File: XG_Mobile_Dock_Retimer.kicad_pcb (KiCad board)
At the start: 4 copper layers, 220.1 x 93 mm, 138 parts, among them J1 5-1775443-8, J10 SWD, J11 UART, J12 I2C1, J13 39301240, J14 SWD, J15 SWD, J17 8730, J2 20455-040E-76, J20 SWD, J21 SWD, J22 SWD, J23 SWD, J24 SWD, J25 SWD, J26 SWD, J27 SWD, J28 SWD, J29 SWD, J3 20455-040E-76, J30 SWD, J31 SWD, J32 SWD, J33 SWD, J4 3-2362375-4, J5 USB_C_Receptacle, J6 455860005, Q16 AO3401A, Q17 2N7002W, SW1 SW_Push, U1 DS160PT801ACBR, U12 STM32F030C8Tx

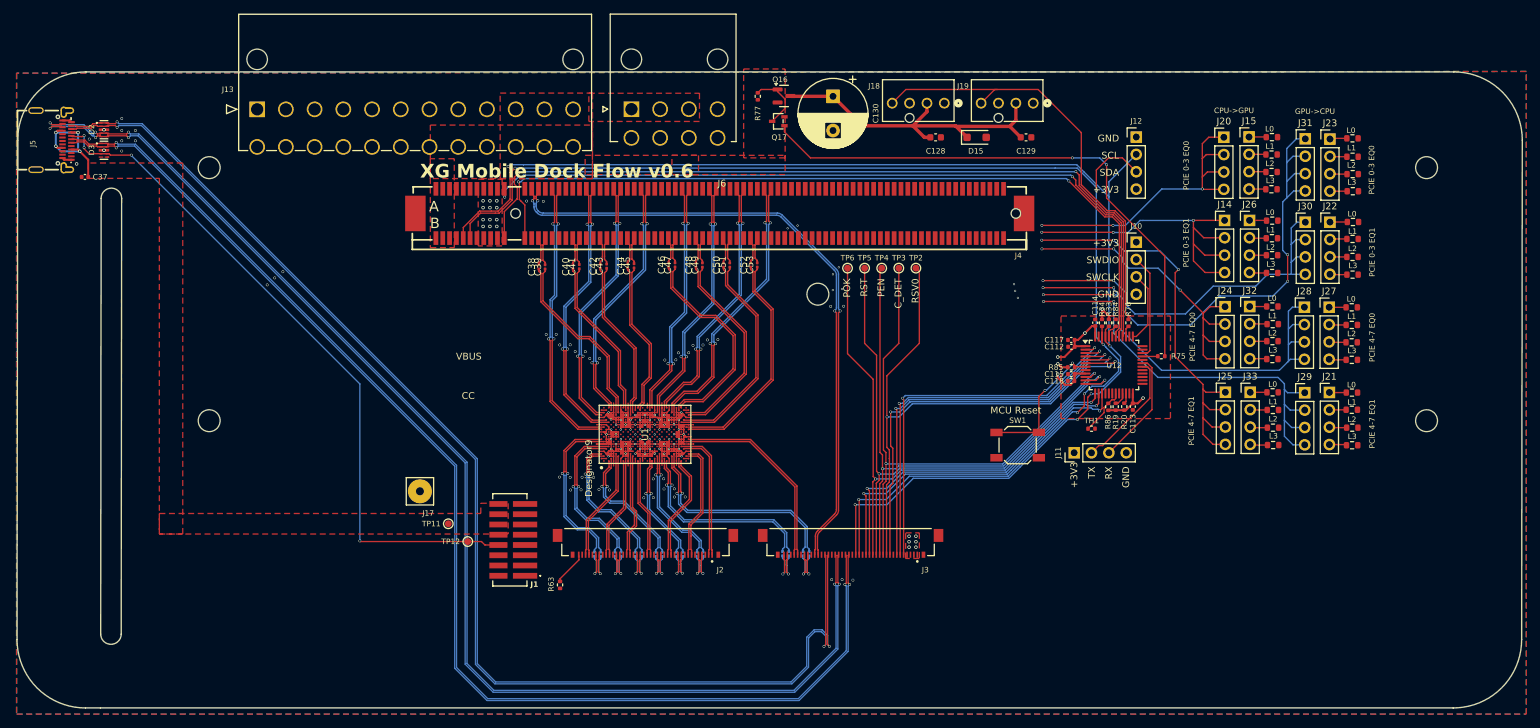
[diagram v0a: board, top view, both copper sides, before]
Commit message: try to route power to retimer
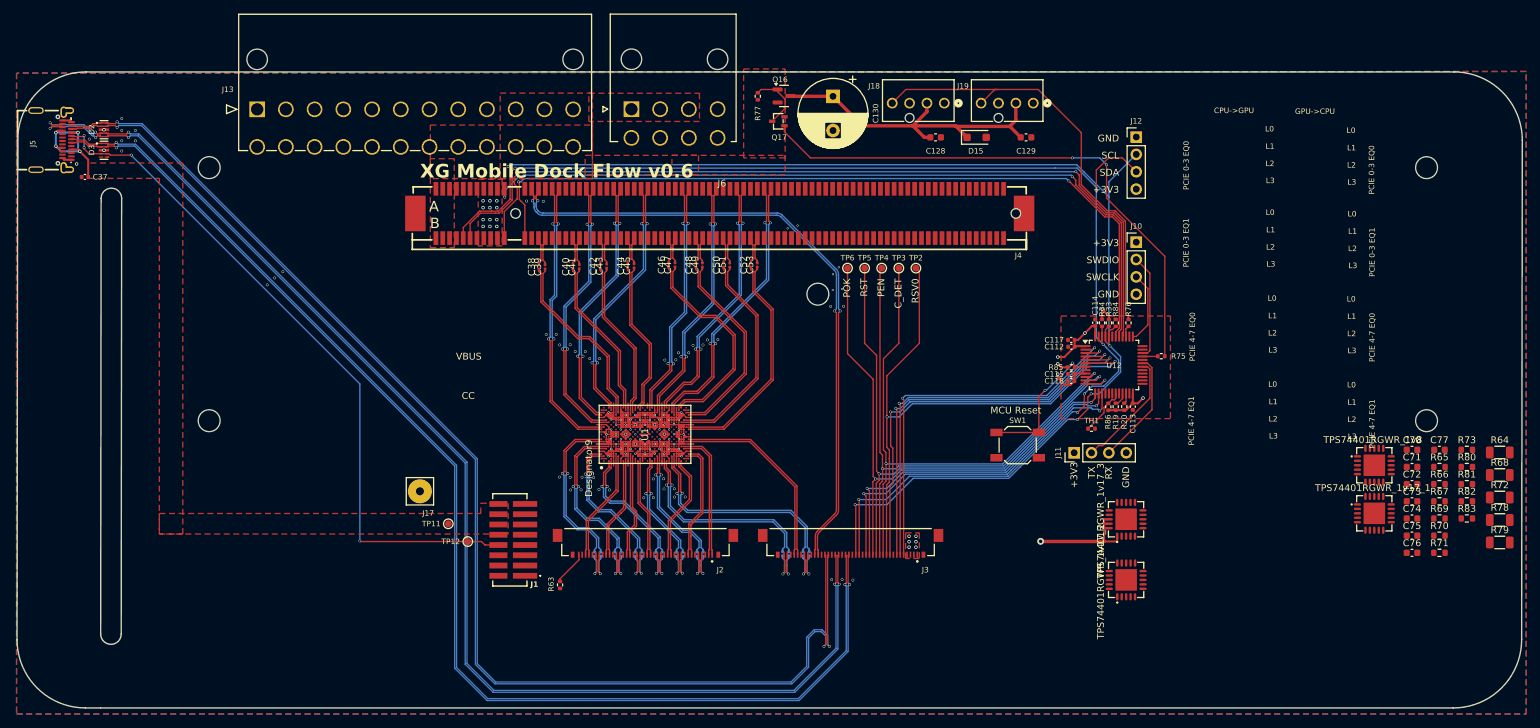
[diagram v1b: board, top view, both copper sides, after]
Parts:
- removed J14, J15, J20, J21, J22, J23, J24, J25, J26, J27, J28, J29, J30, J31, J32, J33: SWD, Connector_PinHeader_2.54mm:PinHeader_1x04_P2.54mm_Vertical
- removed R100, R104, R88, R92, R96: 75k, Resistor_SMD:R_0603_1608Metric
- removed R101, R89, R93, R97: 1k, Resistor_SMD:R_0603_1608Metric
- removed R102, R90, R94, R98: 8.25k, Resistor_SMD:R_0603_1608Metric
- removed R103, R87, R91, R95, R99: 24.9k, Resistor_SMD:R_0603_1608Metric
- added C70: 4.7μF, Capacitor_SMD:C_0603_1608Metric, F.Cu at (220.7, 94.7)
- added C71: 4.7μF, Capacitor_SMD:C_0603_1608Metric, F.Cu at (220.7, 97.2)
- added C72: 4.7μF, Capacitor_SMD:C_0603_1608Metric, F.Cu at (220.7, 99.7)
- added C73: 4.7μF, Capacitor_SMD:C_0603_1608Metric, F.Cu at (220.7, 102.2)
- added C74: 4.7μF, Capacitor_SMD:C_0603_1608Metric, F.Cu at (220.7, 104.7)
- added C75: 4.7μF, Capacitor_SMD:C_0603_1608Metric, F.Cu at (220.7, 107.2)
- added C76: 4.7μF, Capacitor_SMD:C_0603_1608Metric, F.Cu at (220.7, 109.7)
- added C77: 4.7μF, Capacitor_SMD:C_0603_1608Metric, F.Cu at (224.7, 94.7)
- added R64: 1k, Resistor_SMD:R_1206_3216Metric, F.Cu at (233.5, 95.1)
- added R65: 430, Resistor_SMD:R_0603_1608Metric, F.Cu at (224.7, 97.2)
- added TPS74401RGWR_1v17_1: ~, VQFN-20_L5.0-W5.0-P0.65-TL-EP:VQFN-20_L5.0-W5.0-P0.65-TL-EP, F.Cu at (215.2, 104.0)
- added TPS74401RGWR_1v17_2: ~, VQFN-20_L5.0-W5.0-P0.65-TL-EP:VQFN-20_L5.0-W5.0-P0.65-TL-EP, F.Cu at (178.9, 113.7)
- added TPS74401RGWR_1v17_3: ~, VQFN-20_L5.0-W5.0-P0.65-TL-EP:VQFN-20_L5.0-W5.0-P0.65-TL-EP, F.Cu at (178.8, 104.8)
- added TPS74401RGWR_1v8: ~, VQFN-20_L5.0-W5.0-P0.65-TL-EP:VQFN-20_L5.0-W5.0-P0.65-TL-EP, F.Cu at (215.2, 96.9)
- R66, R70: value 1k -> 30
- R67, R71: value 8.25k -> 3
- R68, R72: value 24.9k -> 1k; footprint Resistor_SMD:R_0603_1608Metric -> Resistor_SMD:R_1206_3216Metric
- R69, R73: value 75k -> 430
- R78: footprint Resistor_SMD:R_0603_1608Metric -> Resistor_SMD:R_1206_3216Metric
- R79: value 8.25k -> 1k; footprint Resistor_SMD:R_0603_1608Metric -> Resistor_SMD:R_1206_3216Metric
- R80: value 24.9k -> 30
- R81: value 75k -> 3
- R82: value 1k -> 240
- R83: value 8.25k -> 10
- moved R66 56.3 mm to (224.7, 99.7), turned to 0 degrees
- moved R67 56.3 mm to (224.7, 102.2), turned to 0 degrees
- moved R68 55.5 mm to (233.5, 98.4), turned to 0 degrees
- moved R69 54.0 mm to (224.7, 104.7), turned to 0 degrees
- moved R79 46.1 mm to (233.5, 108.2), turned to 0 degrees
- moved R78 45.6 mm to (233.5, 104.9), turned to 0 degrees
- moved R80 33.9 mm to (228.7, 97.2), turned to 0 degrees
- moved R81 33.8 mm to (228.7, 99.7), turned to 0 degrees
- moved R82 32.6 mm to (228.7, 102.2), turned to 0 degrees
- moved R83 32.5 mm to (228.7, 104.7), turned to 0 degrees
- moved R71 24.5 mm to (224.7, 109.7), turned to 0 degrees
- moved R70 24.5 mm to (224.7, 107.2), turned to 0 degrees
- moved R72 23.9 mm to (233.5, 101.7), turned to 0 degrees
- moved R73 16.8 mm to (228.7, 94.7), turned to 0 degrees
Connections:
- R66 pad 1: GND -> Net-(R65-Pad1)
- R66 pad 2: Net-(J15-Pin_1) -> Net-(R66-Pad2)
- R67 pad 1: GND -> +1V17_1
- R67 pad 2: Net-(J15-Pin_2) -> Net-(R66-Pad2)
- R68 pad 1: GND -> Net-(TPS74401RGWR_1v17_2-FB)
- R68 pad 2: Net-(J15-Pin_3) -> GND
- R69 pad 1: GND -> Net-(R69-Pad1)
- R69 pad 2: Net-(J15-Pin_4) -> Net-(TPS74401RGWR_1v17_2-FB)
- R70 pad 1: GND -> Net-(R69-Pad1)
- R70 pad 2: Net-(J21-Pin_1) -> Net-(R70-Pad2)
- R71 pad 1: GND -> +1V17_2
- R71 pad 2: Net-(J21-Pin_2) -> Net-(R70-Pad2)
- R72 pad 1: GND -> Net-(TPS74401RGWR_1v17_3-FB)
- R72 pad 2: Net-(J21-Pin_3) -> GND
- R73 pad 1: GND -> Net-(R73-Pad1)
- R73 pad 2: Net-(J21-Pin_4) -> Net-(TPS74401RGWR_1v17_3-FB)
- R78 pad 1: GND -> Net-(TPS74401RGWR_1v8-FB)
- R78 pad 2: Net-(J32-Pin_1) -> GND
- R79 pad 1: GND -> Net-(R79-Pad1)
- R79 pad 2: Net-(J32-Pin_2) -> Net-(TPS74401RGWR_1v8-FB)
- R80 pad 1: GND -> Net-(R73-Pad1)
- R80 pad 2: Net-(J32-Pin_3) -> Net-(R80-Pad2)
- R81 pad 1: GND -> +1V17_3
- R81 pad 2: Net-(J32-Pin_4) -> Net-(R80-Pad2)
- R82 pad 1: GND -> Net-(R79-Pad1)
- R82 pad 2: Net-(J33-Pin_1) -> Net-(R82-Pad2)
- R83 pad 1: GND -> +1V8
- R83 pad 2: Net-(J33-Pin_2) -> Net-(R82-Pad2)
- U1 pad AA12: unconnected-(U1F-PWR2_HS_D-PadAA12) -> +1V17_2
- U1 pad AB15: unconnected-(U1F-PWR_2_A-PadAB15) -> +1V17_1
- U1 pad AB17: unconnected-(U1F-PWR_2_A-PadAB17) -> +1V17_1
- U1 pad AB7: unconnected-(U1F-PWR2_HS_A-PadAB7) -> +1V17_3
- U1 pad AB9: unconnected-(U1F-PWR2_HS_A-PadAB9) -> +1V17_3
- U1 pad AC10: unconnected-(U1F-PWR2_HS_D-PadAC10) -> +1V17_2
- U1 pad AC14: unconnected-(U1F-PWR_2_A-PadAC14) -> +1V17_1
- U1 pad AD15: unconnected-(U1F-PWR_2_A-PadAD15) -> +1V17_1
- U1 pad AD17: unconnected-(U1F-PWR_2_A-PadAD17) -> +1V17_1
- U1 pad AD7: unconnected-(U1F-PWR2_HS_A-PadAD7) -> +1V17_3
- U1 pad AD9: unconnected-(U1F-PWR2_HS_A-PadAD9) -> +1V17_3
- U1 pad AE12: unconnected-(U1C-PWR_1-PadAE12) -> +1V8
- U1 pad AF11: unconnected-(U1C-PWR_1-PadAF11) -> +1V8
- U1 pad AF13: unconnected-(U1C-PWR_1-PadAF13) -> +1V8
- U1 pad AG10: unconnected-(U1C-PWR_1-PadAG10) -> +1V8
- U1 pad AG14: unconnected-(U1C-PWR_1-PadAG14) -> +1V8
- U1 pad AH11: unconnected-(U1C-PWR_1-PadAH11) -> +1V8
- U1 pad AH13: unconnected-(U1C-PWR_1-PadAH13) -> +1V8
- U1 pad AJ12: unconnected-(U1C-PWR_1-PadAJ12) -> +1V8
- U1 pad AK15: unconnected-(U1F-PWR2_HS_D-PadAK15) -> +1V17_2
- U1 pad AK17: unconnected-(U1F-PWR2_HS_A-PadAK17) -> +1V17_3
- U1 pad AK7: unconnected-(U1F-PWR2_HS_A-PadAK7) -> +1V17_3
- U1 pad AK9: unconnected-(U1F-PWR2_HS_D-PadAK9) -> +1V17_2
- U1 pad AL10: unconnected-(U1F-PWR2_HS_D-PadAL10) -> +1V17_2
- U1 pad AL14: unconnected-(U1F-PWR2_HS_D-PadAL14) -> +1V17_2
- U1 pad AM15: unconnected-(U1F-PWR2_HS_D-PadAM15) -> +1V17_2
- U1 pad AM17: unconnected-(U1F-PWR2_HS_A-PadAM17) -> +1V17_3
- U1 pad AM7: unconnected-(U1F-PWR2_HS_A-PadAM7) -> +1V17_3
- U1 pad AM9: unconnected-(U1F-PWR2_HS_D-PadAM9) -> +1V17_2
- U1 pad F15: unconnected-(U1F-PWR2_HS_D-PadF15) -> +1V17_2
- U1 pad F17: unconnected-(U1F-PWR2_HS_A-PadF17) -> +1V17_3
- U1 pad F7: unconnected-(U1F-PWR2_HS_A-PadF7) -> +1V17_3
- U1 pad F9: unconnected-(U1F-PWR2_HS_D-PadF9) -> +1V17_2
- U1 pad G10: unconnected-(U1F-PWR2_HS_D-PadG10) -> +1V17_2
- U1 pad G14: unconnected-(U1F-PWR2_HS_D-PadG14) -> +1V17_2
- U1 pad H15: unconnected-(U1F-PWR2_HS_D-PadH15) -> +1V17_2
- U1 pad H17: unconnected-(U1F-PWR2_HS_A-PadH17) -> +1V17_3
- U1 pad H7: unconnected-(U1F-PWR2_HS_A-PadH7) -> +1V17_3
- U1 pad H9: unconnected-(U1F-PWR2_HS_D-PadH9) -> +1V17_2
- U1 pad J12: unconnected-(U1C-PWR_1-PadJ12) -> +1V8
- U1 pad K11: unconnected-(U1C-PWR_1-PadK11) -> +1V8
- U1 pad K13: unconnected-(U1C-PWR_1-PadK13) -> +1V8
- U1 pad L10: unconnected-(U1C-PWR_1-PadL10) -> +1V8
- U1 pad L14: unconnected-(U1C-PWR_1-PadL14) -> +1V8
- U1 pad M11: unconnected-(U1C-PWR_1-PadM11) -> +1V8
- U1 pad M13: unconnected-(U1C-PWR_1-PadM13) -> +1V8
- U1 pad N12: unconnected-(U1C-PWR_1-PadN12) -> +1V8
- U1 pad P15: unconnected-(U1F-PWR2_HS_A-PadP15) -> +1V17_3
- U1 pad P17: unconnected-(U1F-PWR2_HS_A-PadP17) -> +1V17_3
- U1 pad P7: unconnected-(U1F-PWR_2_A-PadP7) -> +1V17_1
- U1 pad P9: unconnected-(U1F-PWR_2_A-PadP9) -> +1V17_1
- U1 pad R10: unconnected-(U1F-PWR_2_A-PadR10) -> +1V17_1
- U1 pad R14: unconnected-(U1F-PWR2_HS_D-PadR14) -> +1V17_2
- U1 pad T15: unconnected-(U1F-PWR2_HS_A-PadT15) -> +1V17_3
- U1 pad T17: unconnected-(U1F-PWR2_HS_A-PadT17) -> +1V17_3
- U1 pad T7: unconnected-(U1F-PWR_2_A-PadT7) -> +1V17_1
- U1 pad T9: unconnected-(U1F-PWR_2_A-PadT9) -> +1V17_1
- U1 pad U12: unconnected-(U1F-PWR2_HS_D-PadU12) -> +1V17_2
- U1 pad V11: unconnected-(U1F-PWR2_HS_D-PadV11) -> +1V17_2
- U1 pad V13: unconnected-(U1F-PWR2_HS_A-PadV13) -> +1V17_3
- U1 pad W10: unconnected-(U1F-PWR2_HS_A-PadW10) -> +1V17_3
- U1 pad W14: unconnected-(U1F-PWR2_HS_A-PadW14) -> +1V17_3
- U1 pad Y11: unconnected-(U1F-PWR2_HS_A-PadY11) -> +1V17_3
- U1 pad Y13: unconnected-(U1F-PWR2_HS_D-PadY13) -> +1V17_2
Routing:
- net +1V17_3: track 0.00 -> 92.0 mm, vias 0 -> 3
- net /GPU_TO_CPU_EQ0_0: track 90.6 -> 0.00 mm, vias 4 -> 0
- net /GPU_TO_CPU_EQ1_1: track 79.5 -> 0.00 mm, vias 2 -> 0
- net /GPU_TO_CPU_EQ0_1: track 77.0 -> 0.00 mm, vias 2 -> 0
- net /GPU_TO_CPU_EQ1_0: track 73.8 -> 0.00 mm, vias 2 -> 0
- net /CPU_TO_GPU_EQ1_1: track 64.9 -> 0.00 mm, vias 3 -> 0
- net /CPU_TO_GPU_EQ1_0: track 51.6 -> 0.00 mm, vias 3 -> 0
- net /CPU_TO_GPU_EQ0_1: track 51.4 -> 0.00 mm, vias 3 -> 0
- net /CPU_TO_GPU_EQ0_0: track 51.3 -> 0.00 mm, vias 3 -> 0
- net +1V8: track 0.00 -> 17.7 mm, vias 0 -> 2
- net +1V17_1: track 0.00 -> 13.1 mm, vias 0 -> 2
- net GND: track 307.8 -> 301.6 mm, vias 127 -> 117
- net Net-(J22-Pin_2): track 2.58 -> 0.00 mm
- net Net-(J33-Pin_4): track 2.57 -> 0.00 mm
- net Net-(J32-Pin_2): track 2.55 -> 0.00 mm
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
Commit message: more changes to power zones
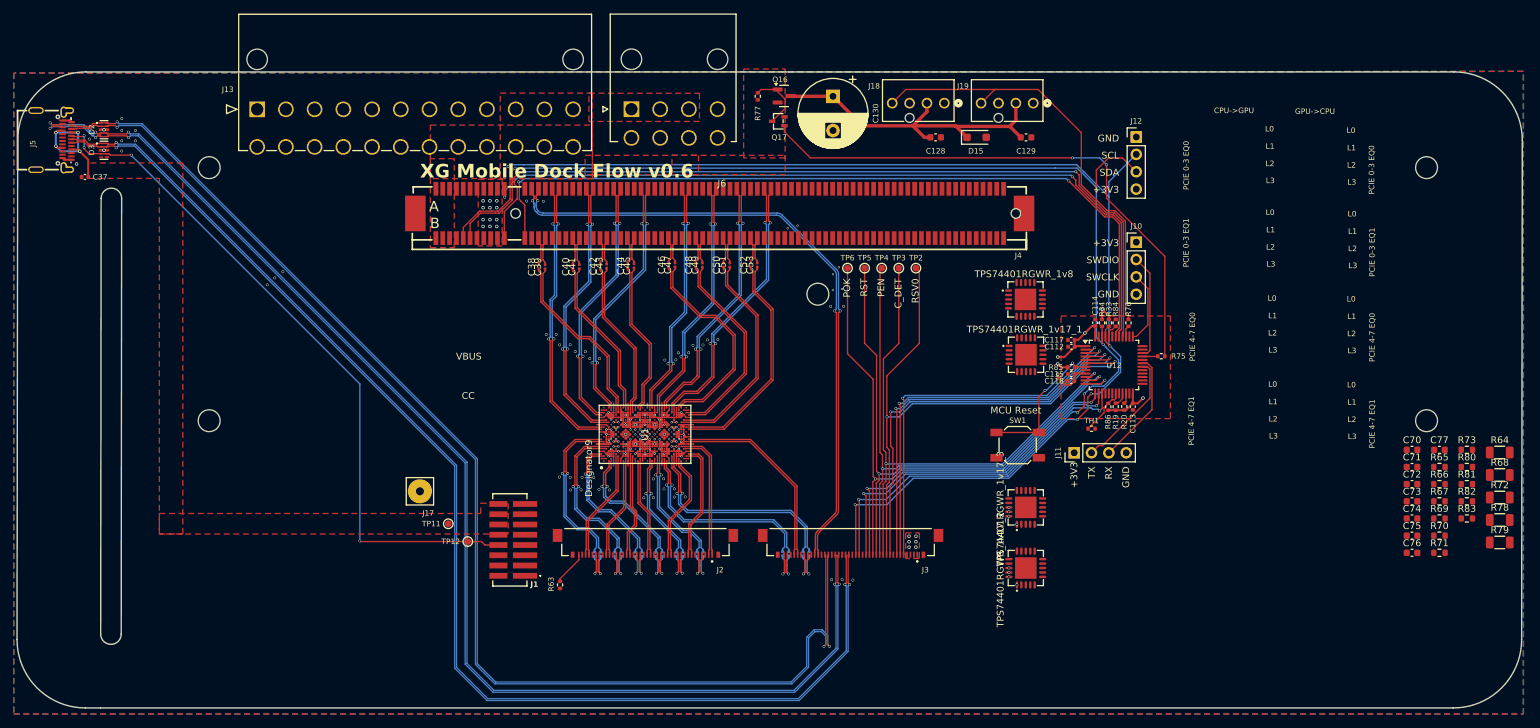
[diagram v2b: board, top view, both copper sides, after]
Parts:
- moved TPS74401RGWR_1v8 56.5 mm to (164.1, 72.7)
- moved TPS74401RGWR_1v17_1 56.0 mm to (164.2, 80.8)
- moved TPS74401RGWR_1v17_2 14.8 mm to (164.2, 112.0)
- moved TPS74401RGWR_1v17_3 14.8 mm to (164.2, 103.1)
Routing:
- net +1V17_3: track 92.0 -> 13.9 mm, vias 3 -> 18
- net GND: track 301.6 -> 252.4 mm, vias 117 -> 113
- net +3V3: track 38.7 -> 29.7 mm
- net +1V17_2: track 2.41 -> 7.91 mm, vias 0 -> 22
- added copper zone on In1.Cu, net +1V17_1
- added copper zone on In3.Cu, net +1V17_2
- added copper zone on In4.Cu, net +1V17_3
- added copper zone on In3.Cu, net GND
- added copper zone on In4.Cu, net GND
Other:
- copper layers 4 -> 6

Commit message: more changes
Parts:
- moved TPS74401RGWR_1v17_2 31.2 mm to (163.2, 80.7)
- moved TPS74401RGWR_1v17_1 31.2 mm to (164.2, 112.0), turned to 90 degrees
- moved TPS74401RGWR_1v8 1.13 mm to (163.1, 73.0), turned to 90 degrees
- moved TPS74401RGWR_1v17_3 0.10 mm to (164.2, 103.2)
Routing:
- net +1V8: vias 2 -> 6
- net +1V17_2: vias 22 -> 20
- net +1V17_1: vias 2 -> 6
- added copper zone on In3.Cu, net +1V17_1
- added copper zone on In4.Cu, net +1V8
- removed copper zone on In1.Cu, net +1V17_1
